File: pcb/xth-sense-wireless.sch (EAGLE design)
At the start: 11 parts, among them CN1 MMG Sensor Input, IC1 OPAMP-DUALDIP

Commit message: updadted schematic.
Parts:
- added C10: 10uF, SparkFun:CAP_POLPTH2
- added C2: 0.47uF, SparkFun:CAPPTH
- added C4: 0.0022uF, SparkFun:CAPPTH
- added C5: 0.022uF, SparkFun:CAPPTH
- added C6, C7, C8: 0.1uF, SparkFun:CAPPTH
- added IC2: MEGA8-P, avr-7:MEGA8-P
- added R7: 4.7K, SparkFun:RESISTORPTH1
- added R8, R9: 235K, SparkFun:RESISTORPTH1
- C3: value (none) -> 0.1uF
- R2: value 200K -> 100K
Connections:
- new net ADC_IN: C5.2, IC1B.-IN, IC1B.OUT, IC2.PC0(ADC0)
- new net N$5: C2.1, R7.2, R8.1
- new net N$6: C10.+, CN1.2
- new net N$7: C4.1, IC1B.+IN, R9.2
- new net N$8: C5.1, R8.2, R9.1
- new net TX: IC2.PD1(TXD)
- net GND: now also C2.2, C4.2, C6.2, C7.2, C8.2, IC2.AGND, IC2.GND@1
- net N$2: now also C10.-; no longer CN1.2
- net N$3: now also R7.1
- net VCC: now also C6.1, C7.1, C8.1, IC2.AVCC, IC2.VCC@1
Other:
- moved on the sheet: BATTERY_POW, C1, C3, CN1, IC1A, IC1B, R1, R2, R3, R4, R5, R6

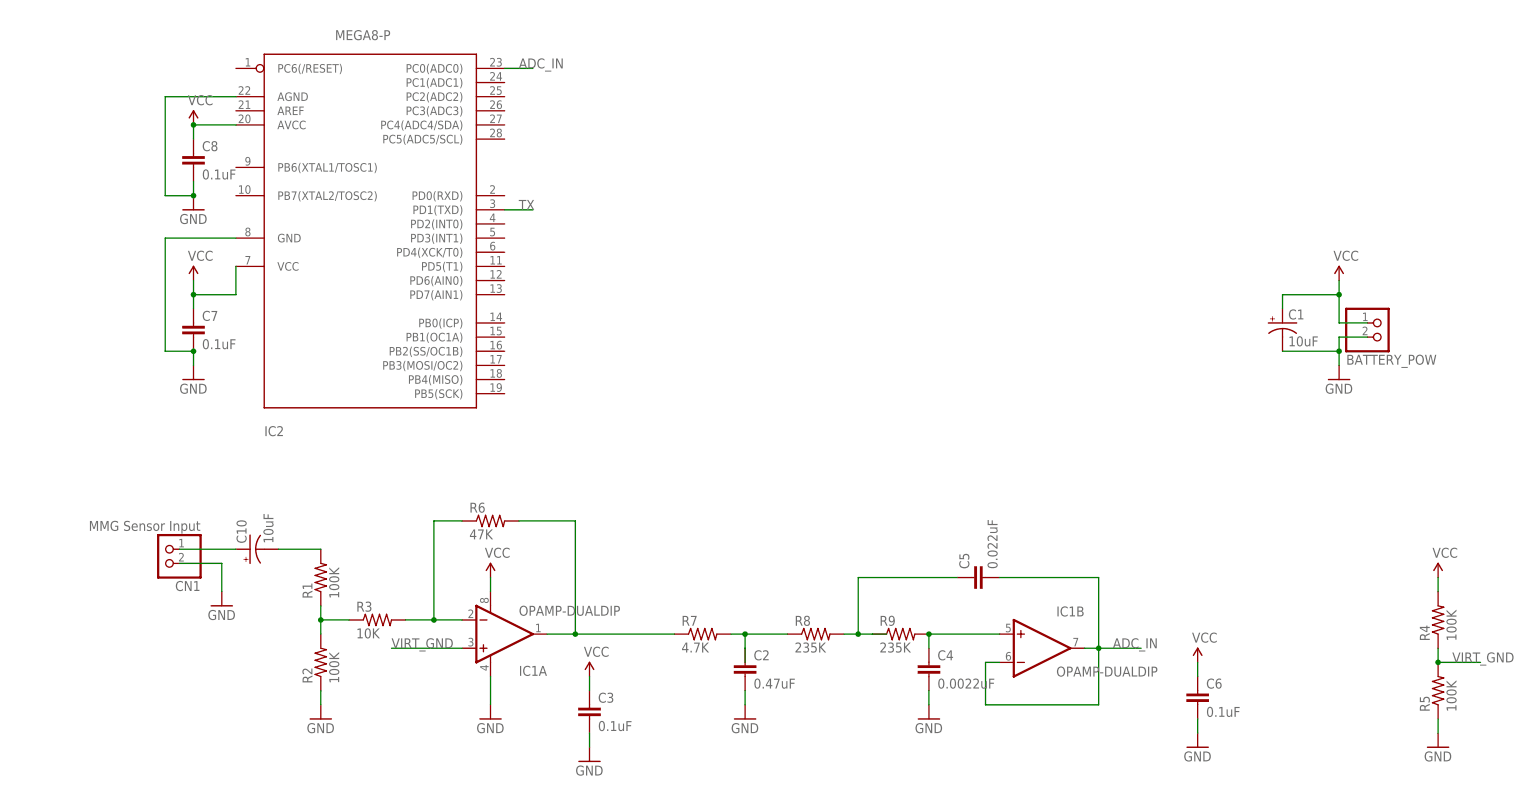
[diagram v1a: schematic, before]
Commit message: fnished schematic nad board layout (except for ground plane in lower-right corner. put one in for the digital grounds…)
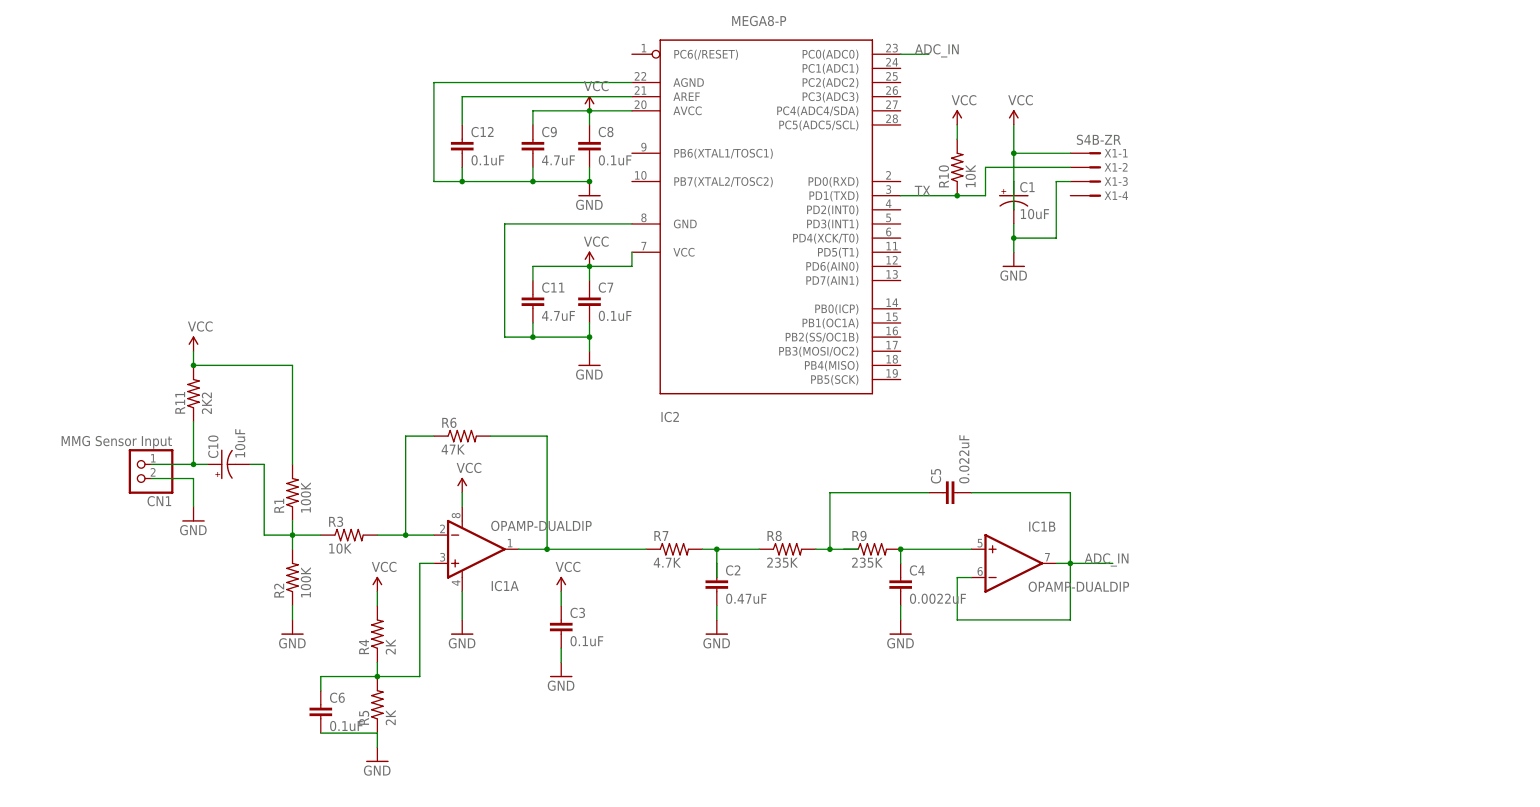
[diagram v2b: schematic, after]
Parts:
- removed BATTERY_POW: (no value), adafruit:JST_2PIN-THM-RA
- added C11, C9: 4.7uF, SparkFun:CAPPTH
- added C12: 0.1uF, SparkFun:CAPPTH
- added R10: 10K, SparkFun:RESISTORPTH1
- added R11: 2K2, SparkFun:RESISTORPTH1
- added X1: S4B-ZR, con-jst:S4B-ZR
- R4, R5: value 100K -> 2K
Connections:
- removed net N$2: C10.-, R1.2
- new net N$9: C12.1, IC2.AREF
- net GND: now also C11.2, C12.2, C9.2, X1-3.1; no longer BATTERY_POW.1
- net N$1: now also C10.-
- net N$6: now also R11.1
- net TX: now also R10.1, X1-2.1
- net VCC: now also C11.1, C9.1, R1.2, R10.2, R11.2, X1-1.1; no longer BATTERY_POW.2, C6.1
- net VIRT_GND: now also C6.1
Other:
- moved on the sheet: C1, C10, C2, C3, C4, C5, C6, C7, C8, CN1, IC1A, IC1B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
